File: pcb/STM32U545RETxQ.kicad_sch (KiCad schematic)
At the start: 19 parts, among them U3 STM32U545RETxQ

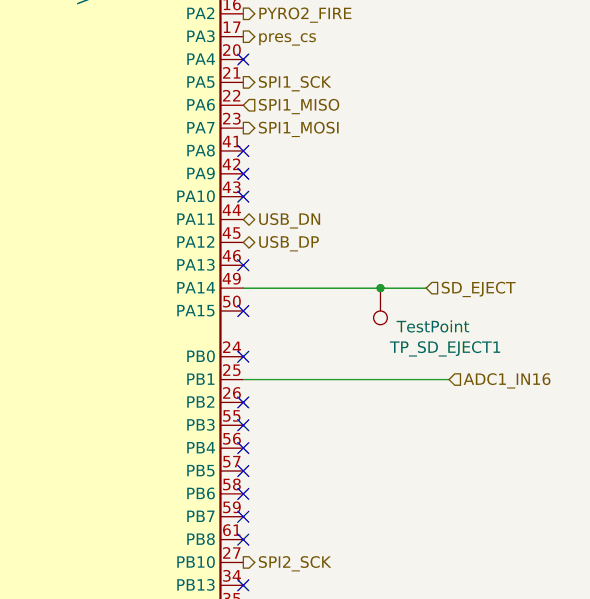
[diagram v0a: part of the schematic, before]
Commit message: Completed most of testbed layout
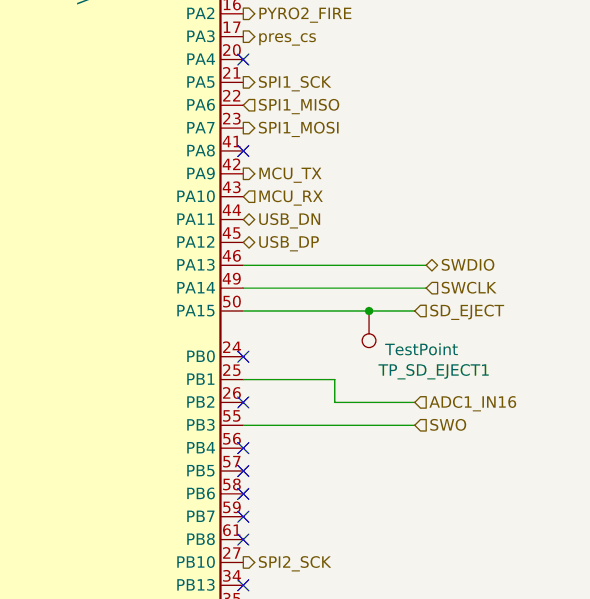
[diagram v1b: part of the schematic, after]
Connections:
- net SD_EJECT: now also U3.50 (PA15); no longer U3.49 (PA14)
- net MCU_TX: now reaches U3.42 (PA9)
- net MCU_RX: now reaches U3.43 (PA10)
- net SWDIO: now reaches U3.46 (PA13)
- net SWO: now reaches U3.55 (PB3)
- new net SWCLK: U3.49 (PA14)
- no-connect marks 25 -> 20
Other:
- moved on the sheet: TP_SD_EJECT1
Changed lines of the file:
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@@
 	)
 	(junction
-		(at 199.39 93.98)
+		(at 198.12 96.52)
 		(diameter 0)
 		(color 0 0 0 0)
@@
 	)
 	(no_connect
-		(at 184.15 96.52)
-	)
-	(no_connect
-		(at 184.15 83.82)
-	)
-	(no_connect
 		(at 133.35 106.68)
 	)
@@
 	)
 	(no_connect
-		(at 184.15 91.44)
-	)
-	(no_connect
 		(at 184.15 116.84)
 	)
@@
 	)
 	(no_connect
-		(at 184.15 81.28)
-	)
-	(no_connect
 		(at 184.15 114.3)
 	)
@@
 	)
 	(no_connect
-		(at 184.15 109.22)
-	)
-	(no_connect
 		(at 133.35 104.14)
 	)
@@
 	(wire
 		(pts
-			(xy 204.47 93.98) (xy 199.39 93.98)
+			(xy 184.15 96.52) (xy 198.12 96.52)
+		)
+		(stroke
+			(width 0)
+			(type default)
+		)
+	)
+	(wire
+		(pts
+			(xy 203.2 96.52) (xy 198.12 96.52)
 		)
 		(stroke
@@
 	(wire
 		(pts
-			(xy 199.39 93.98) (xy 184.15 93.98)
-		)
-		(stroke
-			(width 0)
-			(type default)
-		)
-	)
-	(wire
-		(pts
 			(xy 119.38 73.66) (xy 133.35 73.66)
 		)
@@
 	(wire
 		(pts
+			(xy 184.15 104.14) (xy 194.31 104.14)
+		)
+		(stroke
+			(width 0)
+			(type default)
+		)
+	)
+	(wire
+		(pts
 			(xy 80.01 139.7) (xy 80.01 147.32)
 		)
@@
 	(wire
 		(pts
+			(xy 184.15 93.98) (xy 204.47 93.98)
+		)
+		(stroke
+			(width 0)
+			(type default)
+		)
+	)
+	(wire
+		(pts
 			(xy 151.13 139.7) (xy 151.13 142.24)
 		)
@@
 	(wire
 		(pts
-			(xy 184.15 104.14) (xy 207.01 104.14)
-		)
-		(stroke
-			(width 0)
-			(type default)
-		)
-	)
-	(wire
-		(pts
 			(xy 161.29 139.7) (xy 161.29 142.24)
 		)
@@
 	(wire
 		(pts
+			(xy 194.31 106.68) (xy 203.2 106.68)
+		)
+		(stroke
+			(width 0)
+			(type default)
+		)
+	)
+	(wire
+		(pts
 			(xy 168.91 38.1) (xy 168.91 40.64)
 		)
@@
 	(wire
 		(pts
+			(xy 184.15 109.22) (xy 203.2 109.22)
+		)
+		(stroke
+			(width 0)
+			(type default)
+		)
+	)
+	(wire
+		(pts
 			(xy 156.21 40.64) (xy 156.21 50.8)
 		)
@@
 	(wire
 		(pts
+			(xy 184.15 91.44) (xy 204.47 91.44)
+		)
+		(stroke
+			(width 0)
+			(type default)
+		)
+	)
+	(wire
+		(pts
 			(xy 125.73 58.42) (xy 129.54 58.42)
 		)
@@
 		(pts
 			(xy 156.21 38.1) (xy 156.21 40.64)
+		)
+		(stroke
+			(width 0)
+			(type default)
+		)
+	)
+	(wire
+		(pts
+			(xy 194.31 104.14) (xy 194.31 106.68)
 		)
 		(stroke
@@
 	(hierarchical_label "ADC1_IN16"
 		(shape input)
-		(at 207.01 104.14 0)
+		(at 203.2 106.68 0)
 		(effects
 			(font
@@
 		)
 	)
+	(hierarchical_label "SWO"
+		(shape input)
+		(at 203.2 109.22 0)
+		(effects
+			(font
+				(size 1.27 1.27)
+			)
+			(justify left)
+		)
+	)
 	(hierarchical_label "SD_CMD"
 		(shape output)
@@
 		)
 	)
+	(hierarchical_label "MCU_RX"
+		(shape input)
+		(at 184.15 83.82 0)
+		(effects
+			(font
+				(size 1.27 1.27)
+			)
+			(justify left)
+		)
+	)
+	(hierarchical_label "MCU_TX"
+		(shape output)
+		(at 184.15 81.28 0)
+		(effects
+			(font
+				(size 1.27 1.27)
+			)
+			(justify left)
+		)
+	)
+	(hierarchical_label "SWCLK"
+		(shape input)
+		(at 204.47 93.98 0)
+		(effects
+			(font
+				(size 1.27 1.27)
+			)
+			(justify left)
+		)
+	)
 	(hierarchical_label "ADC1_IN6"
 		(shape input)
@@
 		)
 	)
+	(hierarchical_label "SWDIO"
+		(shape bidirectional)
+		(at 204.47 91.44 0)
+		(effects
+			(font
+				(size 1.27 1.27)
+			)
+			(justify left)
+		)
+	)
 	(hierarchical_label "SD_EJECT"
 		(shape input)
-		(at 204.47 93.98 0)
+		(at 203.2 96.52 0)
 		(effects
 			(font
@@
 	(symbol
 		(lib_id "Connector:TestPoint")
-		(at 199.39 93.98 180)
+		(at 198.12 96.52 180)
 		(unit 1)
 		(exclude_from_sim no)
@@
 		(dnp no)
 		(property "Reference" "TP_SD_EJECT1"
-			(at 212.852 100.584 0)
+			(at 211.582 103.124 0)
 			(effects
 				(font
@@
 		)
 		(property "Value" "TestPoint"
-			(at 209.296 98.298 0)
+			(at 208.026 100.838 0)
 			(effects
 				(font
@@
 		)
 		(property "Footprint" "TestPoint:TestPoint_Loop_D2.54mm_Drill1.5mm_Beaded"
-			(at 194.31 93.98 0)
+			(at 193.04 96.52 0)
 			(effects
 				(font
@@
 		)
 		(property "Datasheet" "https://www.keyelco.com/userAssets/file/M65p56.pdf"
-			(at 194.31 93.98 0)
+			(at 193.04 96.52 0)
 			(effects
 				(font
@@
 		)
 		(property "Description" "test point"
-			(at 199.39 93.98 0)
+			(at 198.12 96.52 0)
 			(effects
 				(font
@@
 		)
 		(property "Purchase" "https://www.digikey.com/en/products/detail/keystone-electronics/5000/255326"
-			(at 199.39 93.98 0)
-			(effects
-				(font
+			(at 198.12 96.52 0)
+			(effects
+				(font

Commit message: Pre-fab update
Pre fab update
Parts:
- renumbered TP_3V3_mcu1 to 3V3_mcu1, TP_BOOT1 to BOOT1, TP_NRST1 to NRST1, TP_SD_EJECT1 to SD_EJECT1, TP_VUSB1 to VDD3V3
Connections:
- net SPI3_SCK: now reaches U3.51 (PC10)
- net SPI3_MISO: now reaches U3.52 (PC11)
- net SPI3_CS: now reaches U3.56 (PB4)
- net SPI3_MOSI: now reaches U3.57 (PB5)
- no-connect marks 20 -> 16
